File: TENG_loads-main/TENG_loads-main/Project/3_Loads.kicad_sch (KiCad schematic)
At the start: 7 parts, among them IC10 TBD62083AFG, IC5 74HC238D,653, IC8 TBD62083AFG

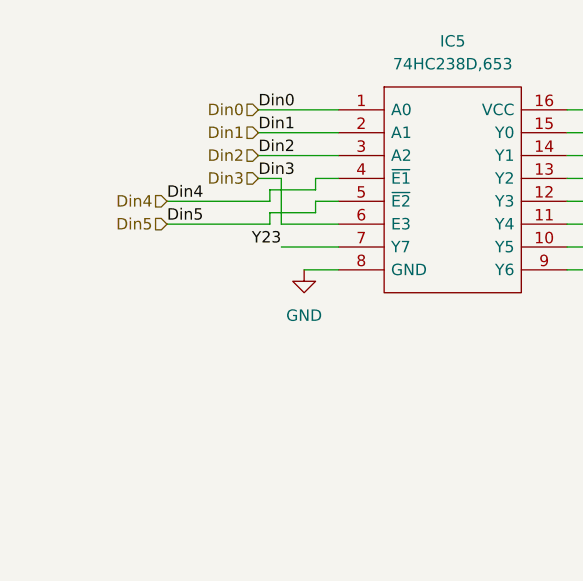
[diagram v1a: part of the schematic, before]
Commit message: Pull Down Resistor and reconnect
Introduced the pull down resistors and reconnect all the unconnected tracks. The position of some items has changed to fit the new components.
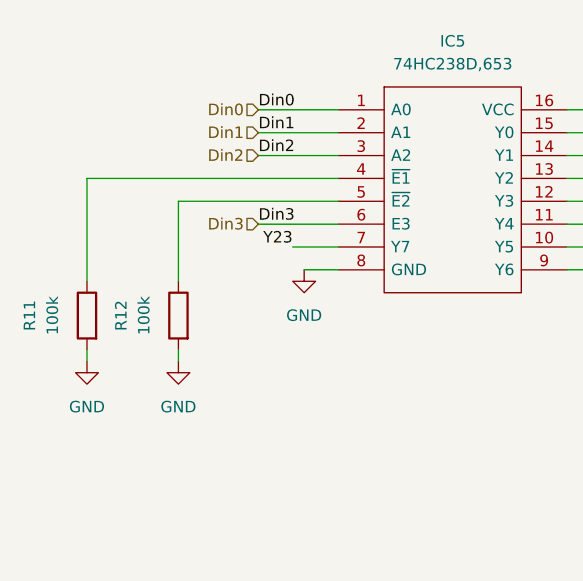
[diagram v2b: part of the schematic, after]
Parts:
- added R11, R12: 100k, Resistor_SMD:R_0805_2012Metric, symbol Device:R
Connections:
- net GND: now also R11.2, R12.2
- net Din4: no longer names the net of IC5.4 (~{E1})
- net Din4: now also R11.1
- net Din5: no longer names the net of IC5.5 (~{E2})
- net Din5: now also R12.1
